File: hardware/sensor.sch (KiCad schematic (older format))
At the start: 10 parts, among them U1 ESP32-WROOM, U2 AP2112K-3.3TRG1, U3 BME280

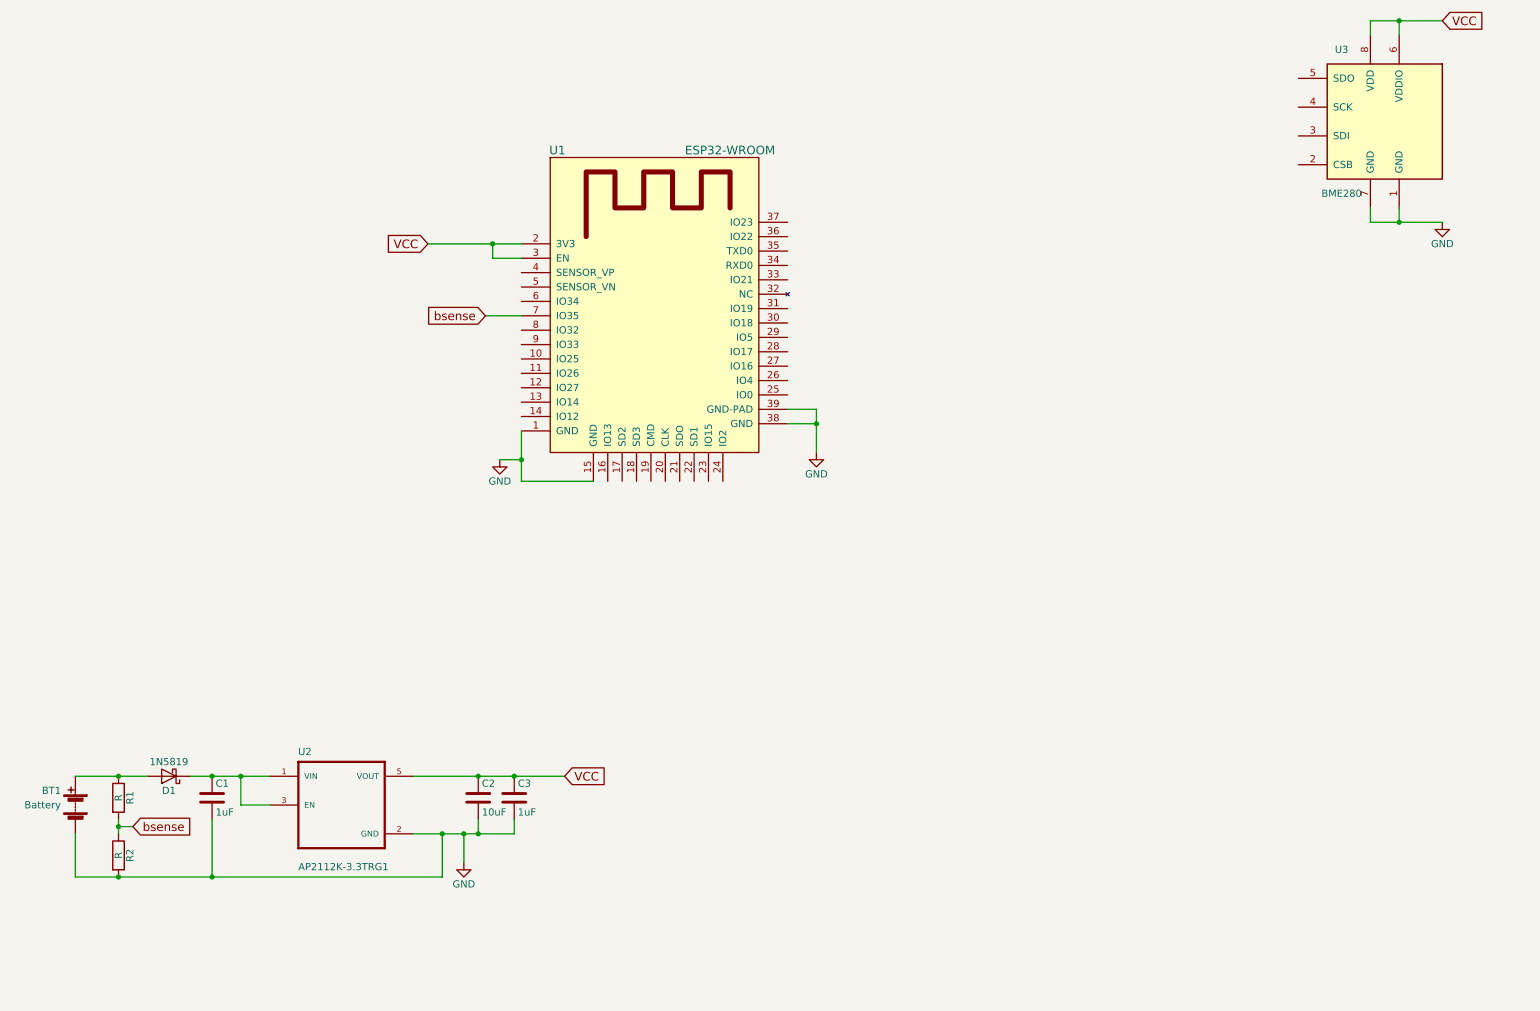
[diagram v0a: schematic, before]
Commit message: Continue schematic work
Cleanup power
Add I2C connectors
Connect BME280 w/ I2C
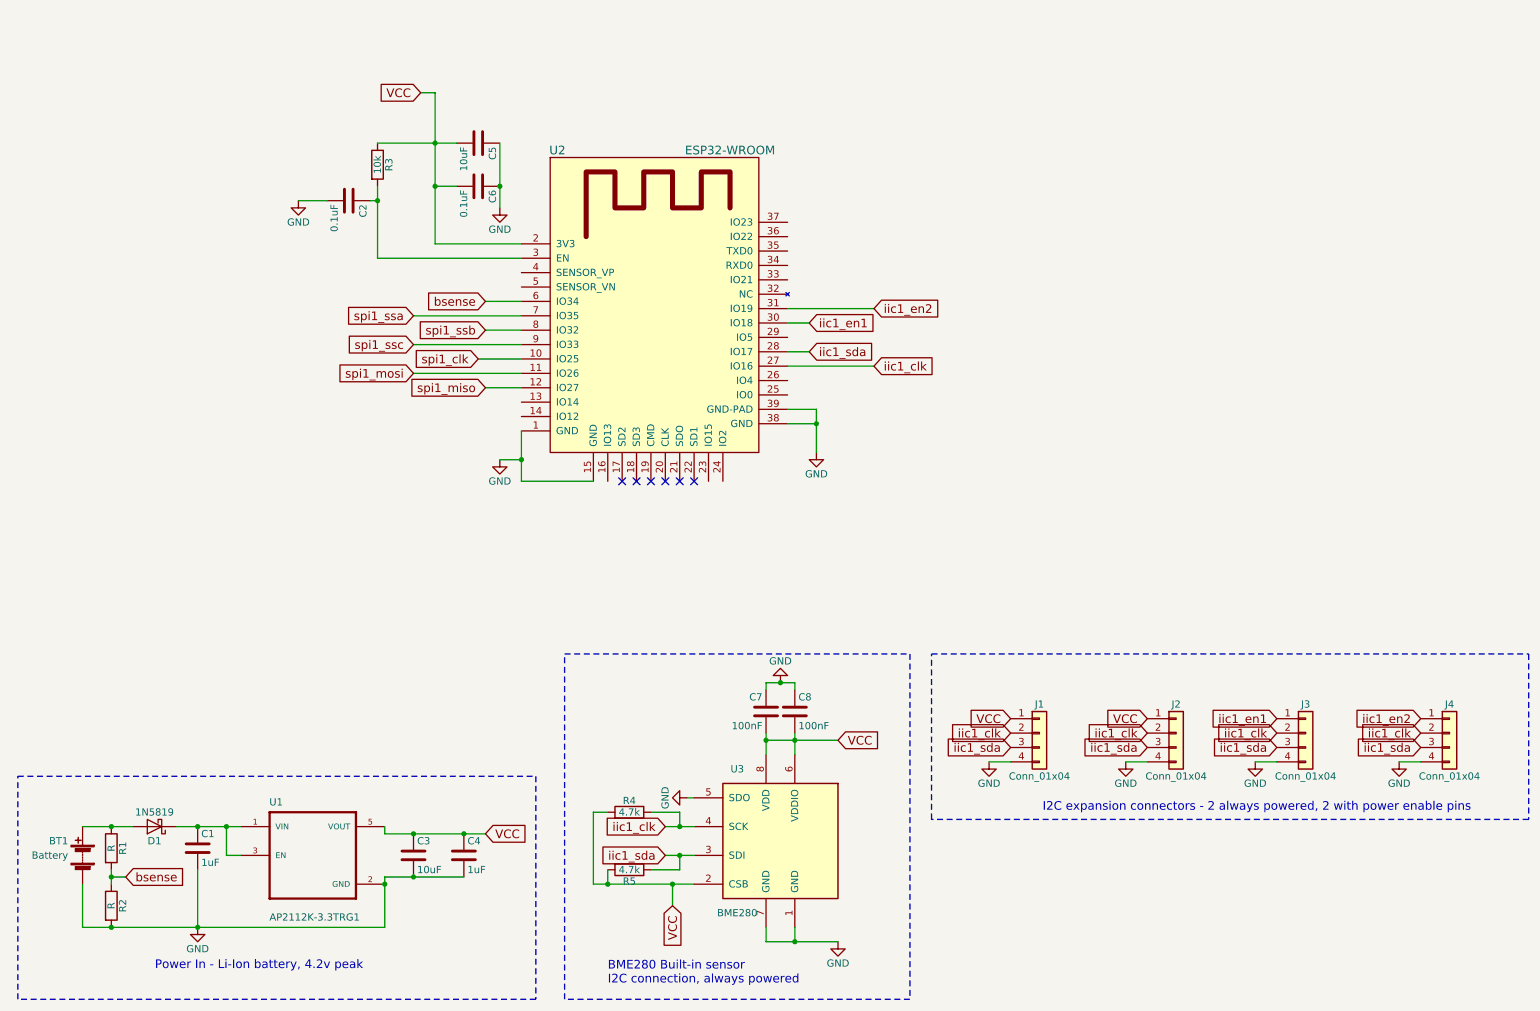
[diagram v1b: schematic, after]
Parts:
- removed U2: AP2112K-3.3TRG1, AP2112K-3.3TRG1:SOT95P285X140-5N, symbol AP2112K-3.3TRG1
- added C4: 1uF, Capacitors_SMD:C_1210, symbol C
- added C5: 10uF, Capacitors_SMD:C_1210, symbol C
- added C6: 0.1uF, Capacitors_SMD:C_1210, symbol C
- added C7, C8: 100nF, Capacitors_SMD:C_1210, symbol C
- added J1, J2, J3, J4: Conn_01x04, Pin_Headers:Pin_Header_Straight_1x04_Pitch1.00mm, symbol Conn_01x04
- added R3: 10k, Resistors_SMD:R_1210, symbol R
- added R4, R5: 4.7k, Resistors_SMD:R_1210, symbol R
- added U1: AP2112K-3.3TRG1, AP2112K-3.3TRG1:SOT95P285X140-5N, symbol AP2112K-3.3TRG1
- C2: value 10uF -> 0.1uF
- C3: value 1uF -> 10uF
- renumbered U1 to U2
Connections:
- net GND: now also U3.5 (SDO), C4.2, C5.1, C6.1, C7.1, C8.1, J1.4 (Pin_4), J2.4 (Pin_4), J3.4 (Pin_4), J4.4 (Pin_4), U1.2 (GND)
- net VCC: now also U3.2 (CSB), C4.1, C5.2, C6.2, C7.2, C8.2, J1.1 (Pin_1), J2.1 (Pin_1), R3.1, R4.2, R5.2, U1.5 (VOUT); no longer C2.1, U2.3 (EN)
- net bsense: now also U2.6 (IO34); no longer U2.7 (IO35)
- net spi1_clk: now reaches U2.10 (IO25)
- net spi1_mosi: now reaches U2.11 (IO26)
- net spi1_miso: now reaches U2.12 (IO27)
- net iic1_clk: now reaches U2.27 (IO16)
- net iic1_clk: now also U3.4 (SCK), J1.2 (Pin_2), J2.2 (Pin_2), J3.2 (Pin_2), J4.2 (Pin_2), R4.1
- net iic1_sda: now reaches U2.28 (IO17)
- net iic1_sda: now also U3.3 (SDI), J1.3 (Pin_3), J2.3 (Pin_3), J3.3 (Pin_3), J4.3 (Pin_3), R5.1
- net iic1_en1: now reaches U2.30 (IO18)
- net iic1_en1: now also J3.1 (Pin_1)
- net iic1_en2: now reaches U2.31 (IO19)
- net iic1_en2: now also J4.1 (Pin_1)
- net spi1_ssb: now reaches U2.8 (IO32)
- net spi1_ssc: now reaches U2.9 (IO33)
- net at C1.1, D1.1 (K): now also U1.1 (VIN), U1.3 (EN)
- new net: C2.1, R3.2, U2.3 (EN)
- new net spi1_ssa: U2.7 (IO35)
- no-connect marks 0 -> 6
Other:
- note added: "BME280 Built-in sensor\nI2C connection, always powered"
- note added: "I2C expansion connectors - 2 always powered, 2 with power enable pins"
- note added: "Power In - Li-Ion battery, 4.2v peak"
- moved on the sheet: U3

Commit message: Continue HW design
* Setup SPI expansion connectors
* Re-annotate caps for power regulator and WROOM power
* Add globals for JTAG pins
* Rough grouping of parts on PCB
- Note - still need to make battery setup choices and footprint choices for passives
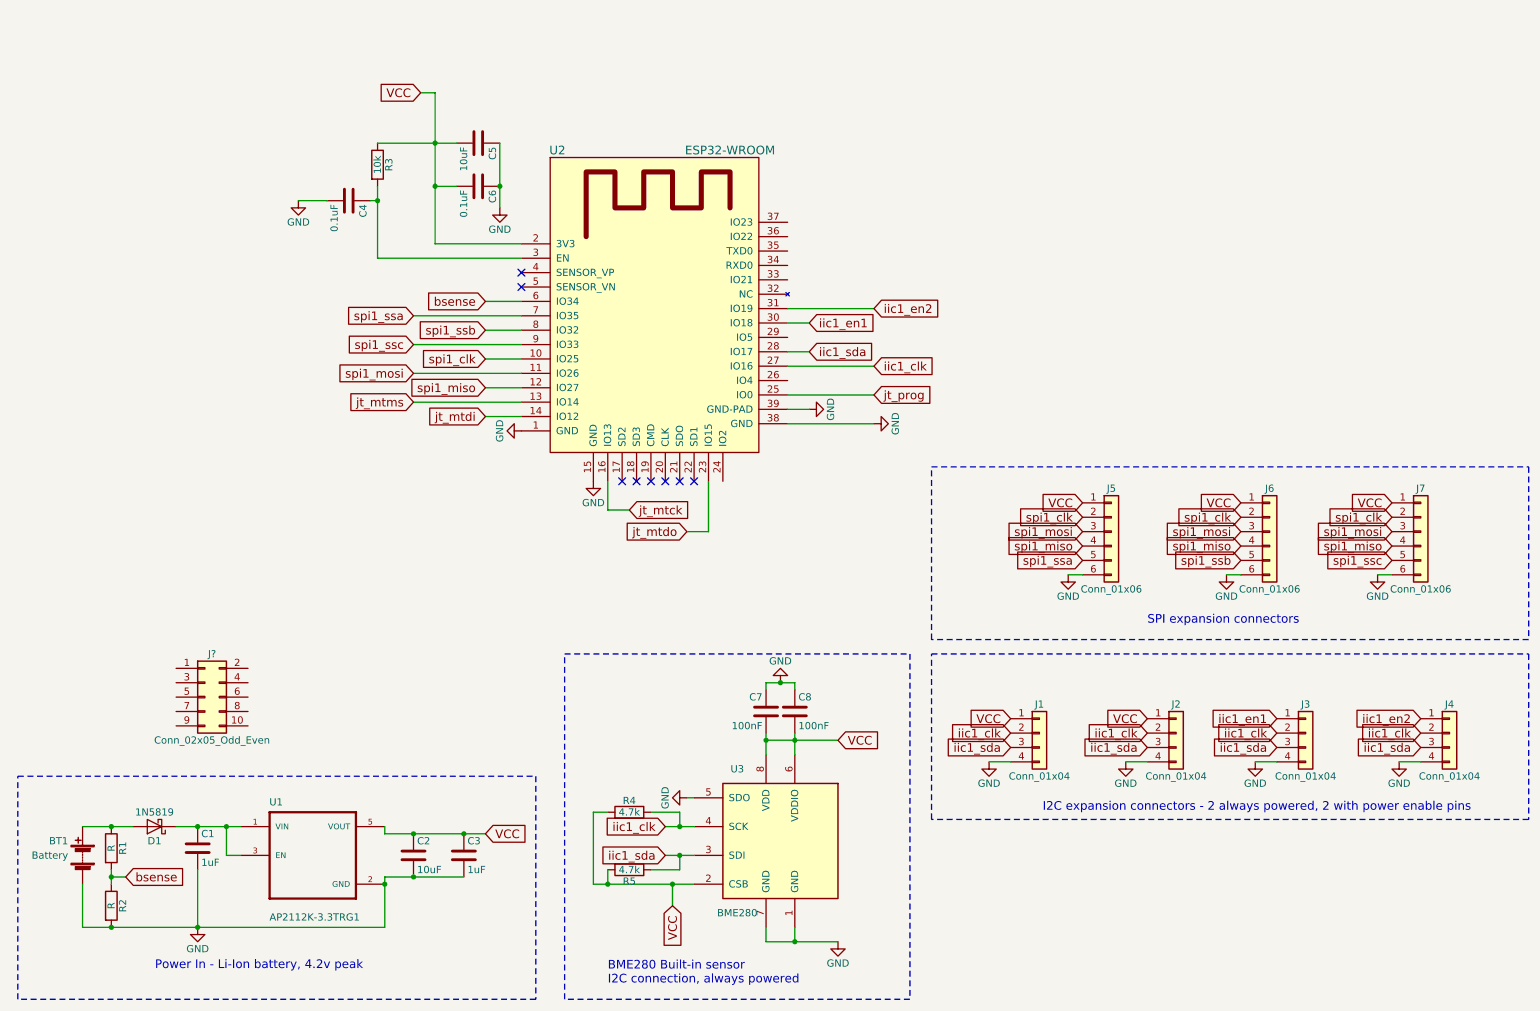
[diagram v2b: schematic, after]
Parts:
- added J5, J6, J7: Conn_01x06, Pin_Headers:Pin_Header_Straight_1x06_Pitch1.00mm, symbol Conn_01x06
- added J?: Conn_02x05_Odd_Even, symbol Conn_02x05_Odd_Even
- renumbered C3 to C2, C4 to C3, C2 to C4
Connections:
- net GND: now also J5.6 (Pin_6), J6.6 (Pin_6), J7.6 (Pin_6)
- net VCC: now also J5.1 (Pin_1), J6.1 (Pin_1), J7.1 (Pin_1)
- net spi1_clk: now also J5.2 (Pin_2), J6.2 (Pin_2), J7.2 (Pin_2)
- net spi1_miso: now also J5.4 (Pin_4), J6.4 (Pin_4), J7.4 (Pin_4)
- net spi1_mosi: now also J5.3 (Pin_3), J6.3 (Pin_3), J7.3 (Pin_3)
- net spi1_ssa: now also J5.5 (Pin_5)
- net spi1_ssb: now also J6.5 (Pin_5)
- net spi1_ssc: now also J7.5 (Pin_5)
- net jt_mtms: now reaches U2.13 (IO14)
- net jt_mtdi: now reaches U2.14 (IO12)
- net jt_mtck: now reaches U2.16 (IO13)
- net jt_mtdo: now reaches U2.23 (IO15)
- net jt_prog: now reaches U2.25 (IO0)
- no-connect marks 6 -> 8
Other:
- note added: "SPI expansion connectors"

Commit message: Sensor board v1 schematic done
* JTAG added
* Keep latest schematic in PDF for easy viewing
* Attempt to fix markdown on hardware description
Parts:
- removed J?: Conn_02x05_Odd_Even, symbol Conn_02x05_Odd_Even
- added J8: Conn_01x06, Pin_Headers:Pin_Header_Straight_1x06_Pitch1.00mm, symbol Conn_01x06
- added JP1: Jumper_NO_Small, Capacitors_SMD:C_0402, symbol Jumper_NO_Small
- BT1: footprint Connectors_JST:JST_EH_B02B-EH-A_02x2.50mm_Straight -> Battery_Holders:Keystone_1042_1x18650
- C1, C2, C3, C4, C5, C6, C7, C8: footprint Capacitors_SMD:C_1210 -> Capacitors_SMD:C_1206
- D1: footprint Diodes_SMD:D_SMA -> Diodes_SMD:D_1206
- R1, R2, R3, R4, R5: footprint Resistors_SMD:R_1210 -> Resistors_SMD:R_1206
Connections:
- net GND: now also J8.5 (Pin_5), JP1.2
- net VCC: now also J8.6 (Pin_6)
- net jt_mtck: now also J8.4 (Pin_4)
- net jt_mtdi: now also J8.2 (Pin_2)
- net jt_mtdo: now also J8.3 (Pin_3)
- net jt_mtms: now also J8.1 (Pin_1)
- net jt_prog: now also JP1.1
- no-connect marks 8 -> 16
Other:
- note added: "Chip VCC filter"
- note added: "Chip powerup RC timer"
- note added: "Enable programming"
- note added: "JTAG Debugging pads"
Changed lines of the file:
@@
 F 0 "C5" H 3825 1850 50  0000 L CNN
 F 1 "10uF" H 3825 1650 50  0000 L CNN
-F 2 "Capacitors_SMD:C_1210" H 3838 1600 50  0001 C CNN
+F 2 "Capacitors_SMD:C_1206" H 3838 1600 50  0001 C CNN
 F 3 "" H 3800 1750 50  0001 C CNN
 	1    3800 1750
@@
 F 0 "C6" H 3825 2150 50  0000 L CNN
 F 1 "0.1uF" H 3825 1950 50  0000 L CNN
-F 2 "Capacitors_SMD:C_1210" H 3838 1900 50  0001 C CNN
+F 2 "Capacitors_SMD:C_1206" H 3838 1900 50  0001 C CNN
 F 3 "" H 3800 2050 50  0001 C CNN
 	1    3800 2050
@@
 F 0 "C4" H 2925 2250 50  0000 L CNN
 F 1 "0.1uF" H 2925 2050 50  0000 L CNN
-F 2 "Capacitors_SMD:C_1210" H 2938 2000 50  0001 C CNN
+F 2 "Capacitors_SMD:C_1206" H 2938 2000 50  0001 C CNN
 F 3 "" H 2900 2150 50  0001 C CNN
 	1    2900 2150
@@
 F 0 "R3" V 3180 1900 50  0000 C CNN
 F 1 "10k" V 3100 1900 50  0000 C CNN
-F 2 "Resistors_SMD:R_1210" V 3030 1900 50  0001 C CNN
+F 2 "Resistors_SMD:R_1206" V 3030 1900 50  0001 C CNN
 F 3 "" H 3100 1900 50  0001 C CNN
 	1    3100 1900
@@
 F 0 "C1" H 1875 6750 50  0000 L CNN
 F 1 "1uF" H 1875 6550 50  0000 L CNN
-F 2 "Capacitors_SMD:C_1210" H 1888 6500 50  0001 C CNN
+F 2 "Capacitors_SMD:C_1206" H 1888 6500 50  0001 C CNN
 F 3 "" H 1850 6650 50  0001 C CNN
 	1    1850 6650
@@
 F 0 "R2" V 1330 7050 50  0000 C CNN
 F 1 "R" V 1250 7050 50  0000 C CNN
-F 2 "Resistors_SMD:R_1210" V 1180 7050 50  0001 C CNN
+F 2 "Resistors_SMD:R_1206" V 1180 7050 50  0001 C CNN
 F 3 "" H 1250 7050 50  0001 C CNN
 	1    1250 7050
@@
 F 0 "R1" V 1330 6650 50  0000 C CNN
 F 1 "R" V 1250 6650 50  0000 C CNN
-F 2 "Resistors_SMD:R_1210" V 1180 6650 50  0001 C CNN
+F 2 "Resistors_SMD:R_1206" V 1180 6650 50  0001 C CNN
 F 3 "" H 1250 6650 50  0001 C CNN
 	1    1250 6650
@@
 F 0 "C3" H 3725 6800 50  0000 L CNN
 F 1 "1uF" H 3725 6600 50  0000 L CNN
-F 2 "Capacitors_SMD:C_1210" H 3738 6550 50  0001 C CNN
+F 2 "Capacitors_SMD:C_1206" H 3738 6550 50  0001 C CNN
 F 3 "" H 3700 6700 50  0001 C CNN
 	1    3700 6700
@@
 F 0 "C2" H 3375 6800 50  0000 L CNN
 F 1 "10uF" H 3375 6600 50  0000 L CNN
-F 2 "Capacitors_SMD:C_1210" H 3388 6550 50  0001 C CNN
+F 2 "Capacitors_SMD:C_1206" H 3388 6550 50  0001 C CNN
 F 3 "" H 3350 6700 50  0001 C CNN
 	1    3350 6700
@@
 F 0 "D1" H 1550 6600 50  0000 C CNN
 F 1 "1N5819" H 1550 6400 50  0000 C CNN
-F 2 "Diodes_SMD:D_SMA" H 1550 6325 50  0001 C CNN
+F 2 "Diodes_SMD:D_1206" H 1550 6325 50  0001 C CNN
 F 3 "" H 1550 6500 50  0001 C CNN
 	1    1550 6500
@@
 F 0 "BT1" H 1150 6800 50  0000 L CNN
 F 1 "Battery" H 1150 6700 50  0000 L CNN
-F 2 "Connectors_JST:JST_EH_B02B-EH-A_02x2.50mm_Straight" V 1050 6760 50  0001 C CNN
+F 2 "Battery_Holders:Keystone_1042_1x18650" V 1050 6760 50  0001 C CNN
 F 3 "" V 1050 6760 50  0001 C CNN
 	1    1050 6700
@@
 F 0 "C7" H 5825 5800 50  0000 L CNN
 F 1 "100nF" H 5825 5600 50  0000 L CNN
-F 2 "Capacitors_SMD:C_1210" H 5838 5550 50  0001 C CNN
+F 2 "Capacitors_SMD:C_1206" H 5838 5550 50  0001 C CNN
 F 3 "" H 5800 5700 50  0001 C CNN
 	1    5800 5700
@@
 F 0 "C8" H 6025 5800 50  0000 L CNN
 F 1 "100nF" H 6025 5600 50  0000 L CNN
-F 2 "Capacitors_SMD:C_1210" H 6038 5550 50  0001 C CNN
+F 2 "Capacitors_SMD:C_1206" H 6038 5550 50  0001 C CNN
 F 3 "" H 6000 5700 50  0001 C CNN
 	1    6000 5700
@@
 F 0 "R4" V 4930 6400 50  0000 C CNN
 F 1 "4.7k" V 4850 6400 50  0000 C CNN
-F 2 "Resistors_SMD:R_1210" V 4780 6400 50  0001 C CNN
+F 2 "Resistors_SMD:R_1206" V 4780 6400 50  0001 C CNN
 F 3 "" H 4850 6400 50  0001 C CNN
 	1    4850 6400
@@
 F 0 "R5" V 4930 6800 50  0000 C CNN
 F 1 "4.7k" V 4850 6800 50  0000 C CNN
-F 2 "Resistors_SMD:R_1210" V 4780 6800 50  0001 C CNN
+F 2 "Resistors_SMD:R_1206" V 4780 6800 50  0001 C CNN
 F 3 "" H 4850 6800 50  0001 C CNN
 	1    4850 6800
@@
 	6550 3500 5950 3500
 $Comp
-L Conn_02x05_Odd_Even J?
-U 1 1 5B3C29B9
-P 1900 5600
-F 0 "J?" H 1950 5900 50  0000 C CNN
-F 1 "Conn_02x05_Odd_Even" H 1950 5300 50  0000 C CNN
-F 2 "" H 1900 5600 50  0001 C CNN
-F 3 "" H 1900 5600 50  0001 C CNN
-	1    1900 5600
-	1    0    0    -1
-$EndComp
+L Conn_01x06 J8
+U 1 1 5B3C465C
+P 1950 5500
+F 0 "J8" H 1950 5800 50  0000 C CNN
+F 1 "Conn_01x06" H 1950 5100 50  0000 C CNN
+F 2 "Pin_Headers:Pin_Header_Straight_1x06_Pitch1.00mm" H 1950 5500 50  0001 C CNN
+F 3 "" H 1950 5500 50  0001 C CNN
+	1    1950 5500
+	1    0    0    -1
+$EndComp
+Text GLabel 1650 5300 0    60   Input ~ 0
+jt_mtms
+Text GLabel 1200 5400 0    60   Input ~ 0
+jt_mtdi
+Text GLabel 1650 5500 0    60   Input ~ 0
+jt_mtdo
+Text GLabel 1200 5600 0    60   Input ~ 0
+jt_mtck
+$Comp
+L GND #PWR018
+U 1 1 5B3C59E8
+P 1650 5700
+F 0 "#PWR018" H 1650 5450 50  0001 C CNN
+F 1 "GND" H 1650 5550 50  0000 C CNN
+F 2 "" H 1650 5700 50  0001 C CNN
+F 3 "" H 1650 5700 50  0001 C CNN
+	1    1650 5700
+	0    1    1    0
+$EndComp
+Text GLabel 1200 5800 0    60   Input ~ 0
+VCC
+Wire Wire Line
+	1650 5300 1750 5300
+Wire Wire Line
+	1750 5400 1200 5400
+Wire Wire Line
+	1200 5600 1750 5600
+Wire Wire Line
+	1750 5500 1650 5500
+Wire Wire Line
+	1650 5700 1750 5700
+Wire Wire Line
+	1750 5800 1200 5800
+Text GLabel 2700 5500 0    60   Input ~ 0
+jt_prog
+$Comp
+L GND #PWR019
+U 1 1 5B3C6E69
+P 3300 5500
+F 0 "#PWR019" H 3300 5250 50  0001 C CNN
+F 1 "GND" H 3300 5350 50  0000 C CNN
+F 2 "" H 3300 5500 50  0001 C CNN
+F 3 "" H 3300 5500 50  0001 C CNN
+	1    3300 5500
+	0    -1   -1   0
+$EndComp
+$Comp
+L Jumper_NO_Small JP1
+U 1 1 5B3C6EFA
+P 3000 5500
+F 0 "JP1" H 3000 5580 50  0000 C CNN
+F 1 "Jumper_NO_Small" H 3010 5440 50  0000 C CNN
+F 2 "Capacitors_SMD:C_0402" H 3000 5500 50  0001 C CNN
+F 3 "" H 3000 5500 50  0001 C CNN
+	1    3000 5500
+	1    0    0    -1
+$EndComp
+Wire Wire Line
+	2700 5500 2900 5500
+Wire Wire Line
+	3100 5500 3300 5500
+Text Notes 2500 5700 0    60   ~ 0
+Enable programming
+Text Notes 1050 6050 0    60   ~ 0
+JTAG Debugging pads
+Wire Notes Line
+	600  6100 600  5150
+Wire Notes Line
+	600  5150 3550 5150
+Wire Notes Line
+	3550 5150 3550 6100
+Wire Notes Line
+	3550 6100 600  6100
+NoConn ~ 5950 2300
+NoConn ~ 5950 2400
+NoConn ~ 5950 2500
+NoConn ~ 5950 2600
+NoConn ~ 5950 2700
+NoConn ~ 5950 3100
+NoConn ~ 5950 3400
+NoConn ~ 5500 4100
+Text Notes 3650 1600 0    60   ~ 0
+Chip VCC filter
+Text Notes 2300 1700 0    60   ~ 0
+Chip powerup RC timer
 $EndSCHEMATC
